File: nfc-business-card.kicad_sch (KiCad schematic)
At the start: 3 parts, among them U1 NT3H2111W0FHKH

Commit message: Fix LA–FD short and XQFN pad orientation before fab.
Route LA around U1, correct side-pad long-axis, add a local VSS island,
and shrink antenna feed pads so DRC no longer reports real copper shorts.
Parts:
- ANT1: footprint NFC_BusinessCard:Antenna_Spiral_84x46_4T -> NFC_BusinessCard:Antenna_Spiral_29x45_5T
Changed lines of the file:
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@@
 		(property "Reference" "ANT1" (at 88.9 71.12 0) (effects (font (size 1.27 1.27))))
 		(property "Value" "Antenna_NFC" (at 88.9 86.36 0) (effects (font (size 1.27 1.27))))
-		(property "Footprint" "NFC_BusinessCard:Antenna_Spiral_84x46_4T" (at 88.9 78.74 0) (effects (font (size 1.27 1.27)) (hide yes)))
+		(property "Footprint" "NFC_BusinessCard:Antenna_Spiral_29x45_5T" (at 88.9 78.74 0) (effects (font (size 1.27 1.27)) (hide yes)))
 		(pin "1")
 		(pin "2")

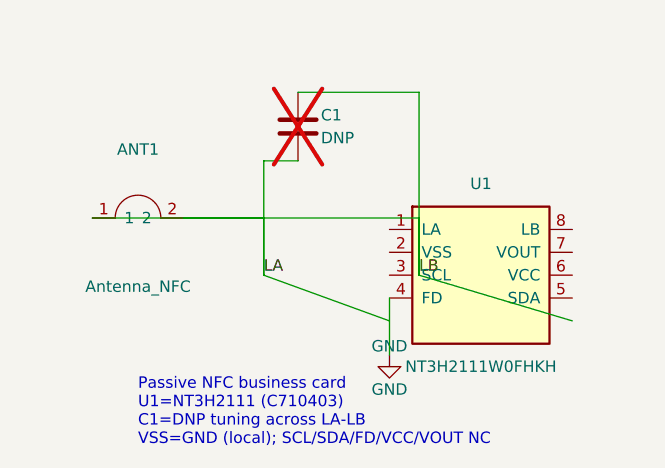
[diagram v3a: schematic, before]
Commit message: Clean schematic ERC with NC marks and net labels.
Connect LA/LB on-grid via labels, mark unused pins no-connect, treat VSS as
passive local ground with PWR_FLAG, and document C1 10–22 pF trim range.
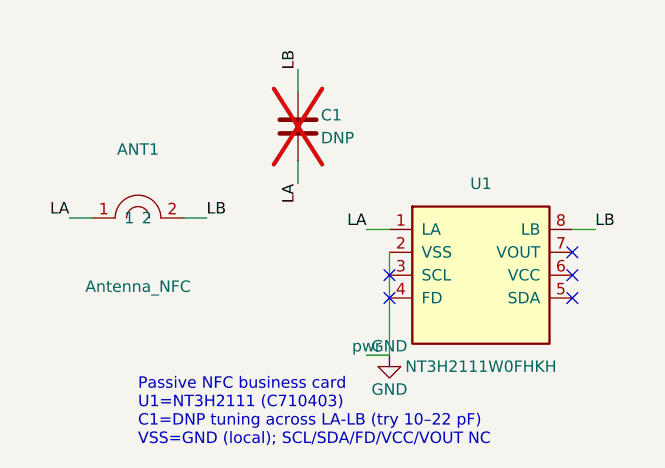
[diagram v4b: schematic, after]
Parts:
- removed C1: DNP, NFC_BusinessCard:C_0402_1005Metric, symbol Device:C
- added C1: DNP, NFC_BusinessCard:C_0402_1005Metric, symbol NFC_BusinessCard:C_0402
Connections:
- net GND: now also U1.2 (VSS); no longer U1.4 (FD)
- net LA: now also U1.1 (LA), C1.2; no longer ANT1.2
- net LB: now reaches U1.8 (LB)
- net LB: now also ANT1.2, C1.1
- no-connect marks 0 -> 5
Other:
- note added: "Passive NFC business card U1=NT3H2111 (C710403) C1=DNP tuning across LA-LB (try 10–22 pF) VSS=GND (local); SCL/SDA/FD/VCC/VOUT NC"
- note removed: "Passive NFC business card U1=NT3H2111 (C710403) C1=DNP tuning across LA-LB VSS=GND (local); SCL/SDA/FD/VCC/VOUT NC"
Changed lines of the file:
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@@
 	)
 	(symbol
-		(lib_id "Device:C")
+		(lib_id "NFC_BusinessCard:C_0402")
 		(at 106.68 68.58 0)
 		(unit 1)
@@
 		(instances (project "nfc-business-card" (path "/db0e1d12-1252-490b-9c29-4e9a9001ab69" (reference "C1") (unit 1))))
 	)
-	(wire (pts (xy 83.82 78.74) (xy 102.87 78.74)) (stroke (width 0) (type default)))
-	(wire (pts (xy 102.87 78.74) (xy 102.87 85.09)) (stroke (width 0) (type default)))
-	(wire (pts (xy 102.87 85.09) (xy 116.84 90.17)) (stroke (width 0) (type default)))
-	(wire (pts (xy 106.68 72.39) (xy 102.87 72.39)) (stroke (width 0) (type default)))
-	(wire (pts (xy 102.87 72.39) (xy 102.87 85.09)) (stroke (width 0) (type default)))
-	(wire (pts (xy 93.98 78.74) (xy 120.13 78.74)) (stroke (width 0) (type default)))
-	(wire (pts (xy 120.13 78.74) (xy 120.13 85.09)) (stroke (width 0) (type default)))
-	(wire (pts (xy 120.13 85.09) (xy 137.16 90.17)) (stroke (width 0) (type default)))
-	(wire (pts (xy 106.68 64.77) (xy 120.13 64.77)) (stroke (width 0) (type default)))
-	(wire (pts (xy 120.13 64.77) (xy 120.13 85.09)) (stroke (width 0) (type default)))
-	(wire (pts (xy 116.84 87.63) (xy 116.84 93.98)) (stroke (width 0) (type default)))
 	(symbol
 		(lib_id "NFC_BusinessCard:GND")
@@
 		(instances (project "nfc-business-card" (path "/db0e1d12-1252-490b-9c29-4e9a9001ab69" (reference "#PWR01") (unit 1))))
 	)
-	(label "LA" (at 102.87 85.09 0) (effects (font (size 1.27 1.27)) (justify left bottom)))
-	(label "LB" (at 120.13 85.09 0) (effects (font (size 1.27 1.27)) (justify left bottom)))
-	(text "Passive NFC business card\nU1=NT3H2111 (C710403)\nC1=DNP tuning across LA-LB\nVSS=GND (local); SCL/SDA/FD/VCC/VOUT NC"
+	(symbol
+		(lib_id "NFC_BusinessCard:PWR_FLAG")
+		(at 114.3 93.98 0)
+		(unit 1)
+		(exclude_from_sim no)
+		(in_bom no)
+		(on_board no)
+		(dnp no)
+		(property "Reference" "#FLG01" (at 114.3 91.44 0) (effects (font (size 1.27 1.27)) (hide yes)))
+		(property "Value" "PWR_FLAG" (at 114.3 91.44 0) (effects (font (size 1.27 1.27)) (hide yes)))
+		(property "Footprint" "" (at 114.3 93.98 0) (effects (font (size 1.27 1.27)) (hide yes)))
+		(pin "1")
+		(instances (project "nfc-business-card" (path "/db0e1d12-1252-490b-9c29-4e9a9001ab69" (reference "#FLG01") (unit 1))))
+	)
+	(wire (pts (xy 83.82 78.74) (xy 81.28 78.74)) (stroke (width 0) (type default)))
+	(label "LA" (at 81.28 78.74 180) (effects (font (size 1.27 1.27)) (justify right bottom)))
+	(wire (pts (xy 116.84 80.01) (xy 114.3 80.01)) (stroke (width 0) (type default)))
+	(label "LA" (at 114.3 80.01 180) (effects (font (size 1.27 1.27)) (justify right bottom)))
+	(wire (pts (xy 106.68 72.39) (xy 106.68 74.93)) (stroke (width 0) (type default)))
+	(label "LA" (at 106.68 74.93 270) (effects (font (size 1.27 1.27)) (justify right bottom)))
+	(wire (pts (xy 93.98 78.74) (xy 96.52 78.74)) (stroke (width 0) (type default)))
+	(label "LB" (at 96.52 78.74 0) (effects (font (size 1.27 1.27)) (justify left bottom)))
+	(wire (pts (xy 137.16 80.01) (xy 139.7 80.01)) (stroke (width 0) (type default)))
+	(label "LB" (at 139.7 80.01 0) (effects (font (size 1.27 1.27)) (justify left bottom)))
+	(wire (pts (xy 106.68 64.77) (xy 106.68 62.23)) (stroke (width 0) (type default)))
+	(label "LB" (at 106.68 62.23 90) (effects (font (size 1.27 1.27)) (justify left bottom)))
+	(wire (pts (xy 116.84 82.55) (xy 116.84 93.98)) (stroke (width 0) (type default)))
+	(wire (pts (xy 116.84 93.98) (xy 114.3 93.98)) (stroke (width 0) (type default)))
+	(no_connect (at 116.84 85.09))
+	(no_connect (at 116.84 87.63))
+	(no_connect (at 137.16 82.55))
+	(no_connect (at 137.16 85.09))
+	(no_connect (at 137.16 87.63))
+	(text "Passive NFC business card\nU1=NT3H2111 (C710403)\nC1=DNP tuning across LA-LB (try 10–22 pF)\nVSS=GND (local); SCL/SDA/FD/VCC/VOUT NC"
 		(at 88.9 104.14 0)
 		(effects (font (size 1.27 1.27)) (justify left bottom))

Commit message: fix(antenna): net coil as F.Cu tracks; footprint is now a net-tie junction
The spiral was un-netted fp_line copper inside the Antenna_Spiral footprint,
making DRC shorting results UUID-dependent (0/1/2 errors across
regenerations). Draw the coil as netted F.Cu tracks (net LA) in write_pcb and
reduce the footprint to a net-tie junction (net_tie_pad_groups "1,2"):
pad 1 = LA at the coil inner end, pad 2 = LB at the B.Cu underpass take-off.
kicad-cli DRC is now 0 violations, deterministic across 5 regenerations.

Also align C1 (DNP 0402) lib/board footprint (exclude_from_bom, DNP F.Fab
value, LCSC Part # C158992, F.Fab lines) clearing the lib_footprint_mismatch
warning; convert LA/LB schematic labels to global labels (clears 6 parity
net_conflicts) and swap C1 wiring to pin1=LA/pin2=LB; extend check_layout.py
with coil LA/LB overlap + net-tie pad checks; document the no-un-netted-copper
rule in AGENTS.md and antenna/NOTES.md; refresh fab outputs.
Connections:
- net LA: now also C1.1; no longer C1.2
- net LB: now also C1.2; no longer C1.1
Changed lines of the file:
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@@
 	)
 	(wire (pts (xy 83.82 78.74) (xy 81.28 78.74)) (stroke (width 0) (type default)))
-	(label "LA" (at 81.28 78.74 180) (effects (font (size 1.27 1.27)) (justify right bottom)))
+	(global_label "LA" (shape input) (at 81.28 78.74 180) (effects (font (size 1.27 1.27)) (justify right bottom)))
 	(wire (pts (xy 116.84 80.01) (xy 114.3 80.01)) (stroke (width 0) (type default)))
-	(label "LA" (at 114.3 80.01 180) (effects (font (size 1.27 1.27)) (justify right bottom)))
+	(global_label "LA" (shape input) (at 114.3 80.01 180) (effects (font (size 1.27 1.27)) (justify right bottom)))
 	(wire (pts (xy 106.68 72.39) (xy 106.68 74.93)) (stroke (width 0) (type default)))
-	(label "LA" (at 106.68 74.93 270) (effects (font (size 1.27 1.27)) (justify right bottom)))
+	(global_label "LB" (shape input) (at 106.68 74.93 270) (effects (font (size 1.27 1.27)) (justify right bottom)))
 	(wire (pts (xy 93.98 78.74) (xy 96.52 78.74)) (stroke (width 0) (type default)))
-	(label "LB" (at 96.52 78.74 0) (effects (font (size 1.27 1.27)) (justify left bottom)))
+	(global_label "LB" (shape input) (at 96.52 78.74 0) (effects (font (size 1.27 1.27)) (justify left bottom)))
 	(wire (pts (xy 137.16 80.01) (xy 139.7 80.01)) (stroke (width 0) (type default)))
-	(label "LB" (at 139.7 80.01 0) (effects (font (size 1.27 1.27)) (justify left bottom)))
+	(global_label "LB" (shape input) (at 139.7 80.01 0) (effects (font (size 1.27 1.27)) (justify left bottom)))
 	(wire (pts (xy 106.68 64.77) (xy 106.68 62.23)) (stroke (width 0) (type default)))
-	(label "LB" (at 106.68 62.23 90) (effects (font (size 1.27 1.27)) (justify left bottom)))
+	(global_label "LA" (shape input) (at 106.68 62.23 90) (effects (font (size 1.27 1.27)) (justify left bottom)))
 	(wire (pts (xy 116.84 82.55) (xy 116.84 93.98)) (stroke (width 0) (type default)))
 	(wire (pts (xy 116.84 93.98) (xy 114.3 93.98)) (stroke (width 0) (type default)))
